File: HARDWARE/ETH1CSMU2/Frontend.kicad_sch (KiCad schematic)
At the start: 76 parts, among them Q601 MMBT3904, Q602 MMBT3904, Q603 MMBT3904, Q604 MMBT3904, U601 DG419DY, U602 DG419DY, U603 SN74LVC1T45DRLR, U604 SN74LVC1T45DRLR, U605 SN74LVC1T45DRLR, U606 LT1970ACFE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

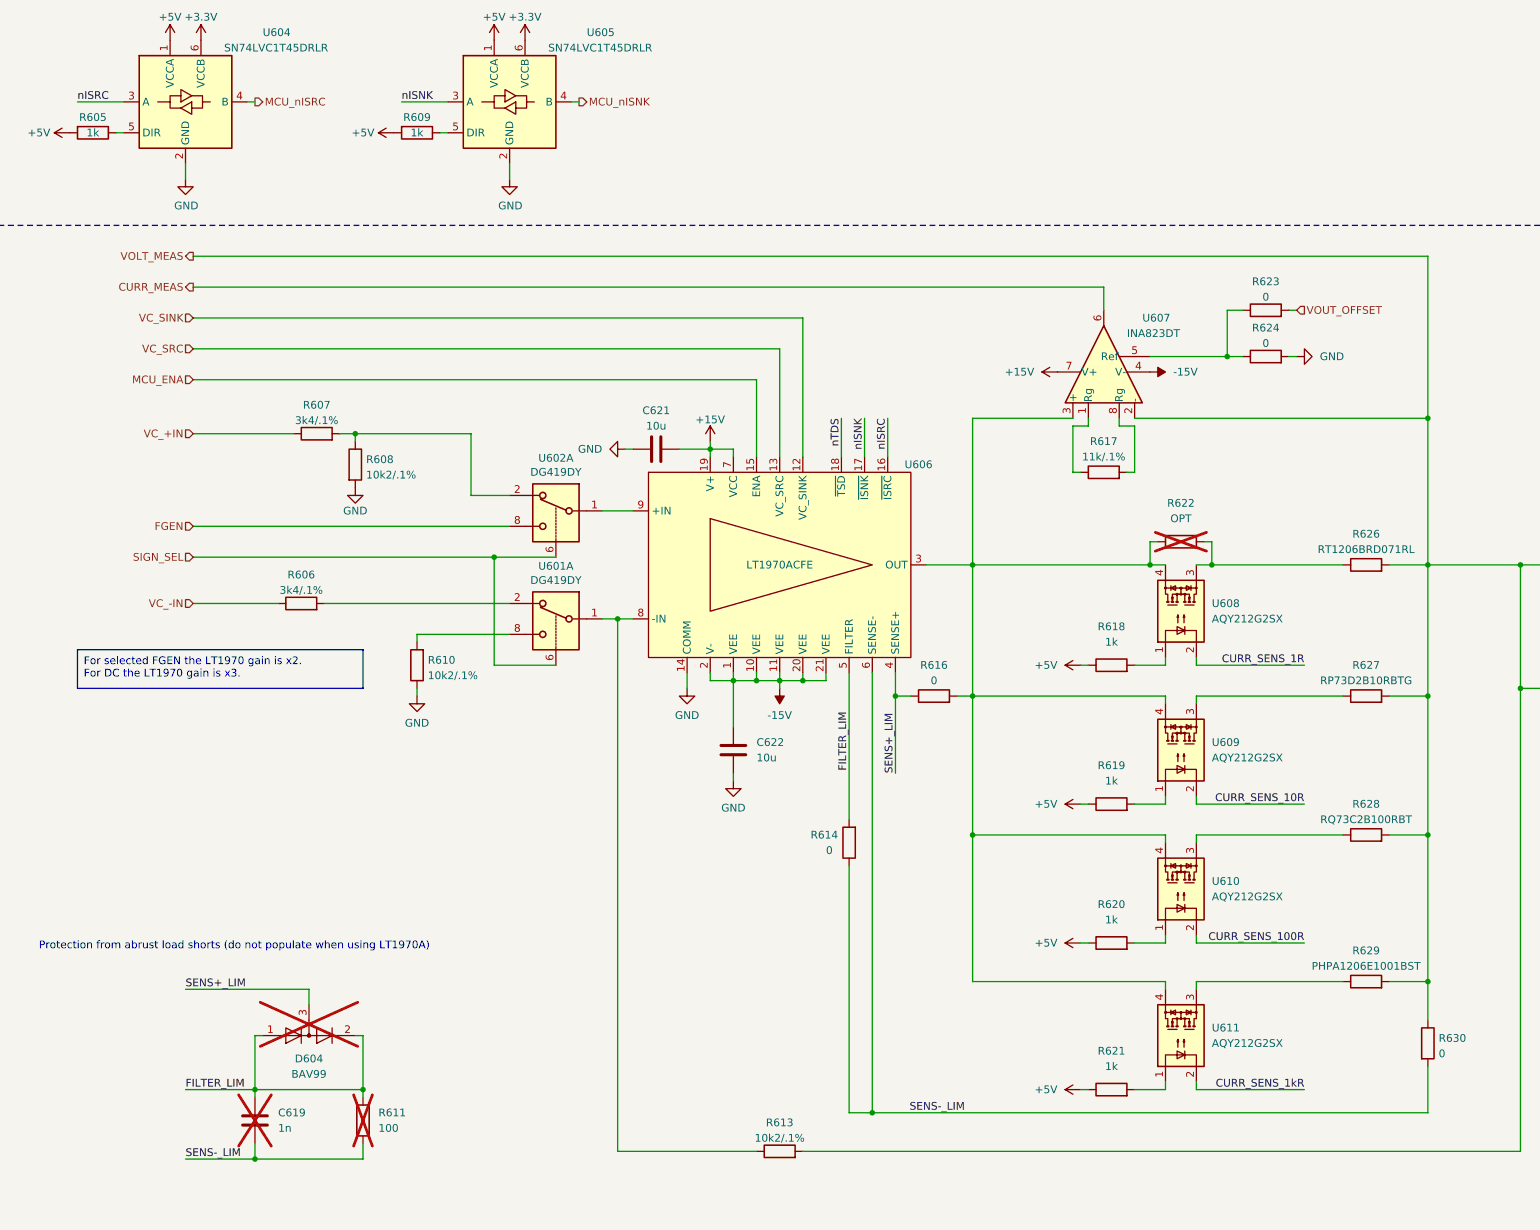
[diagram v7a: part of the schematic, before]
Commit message: Hardware fix. Created README file
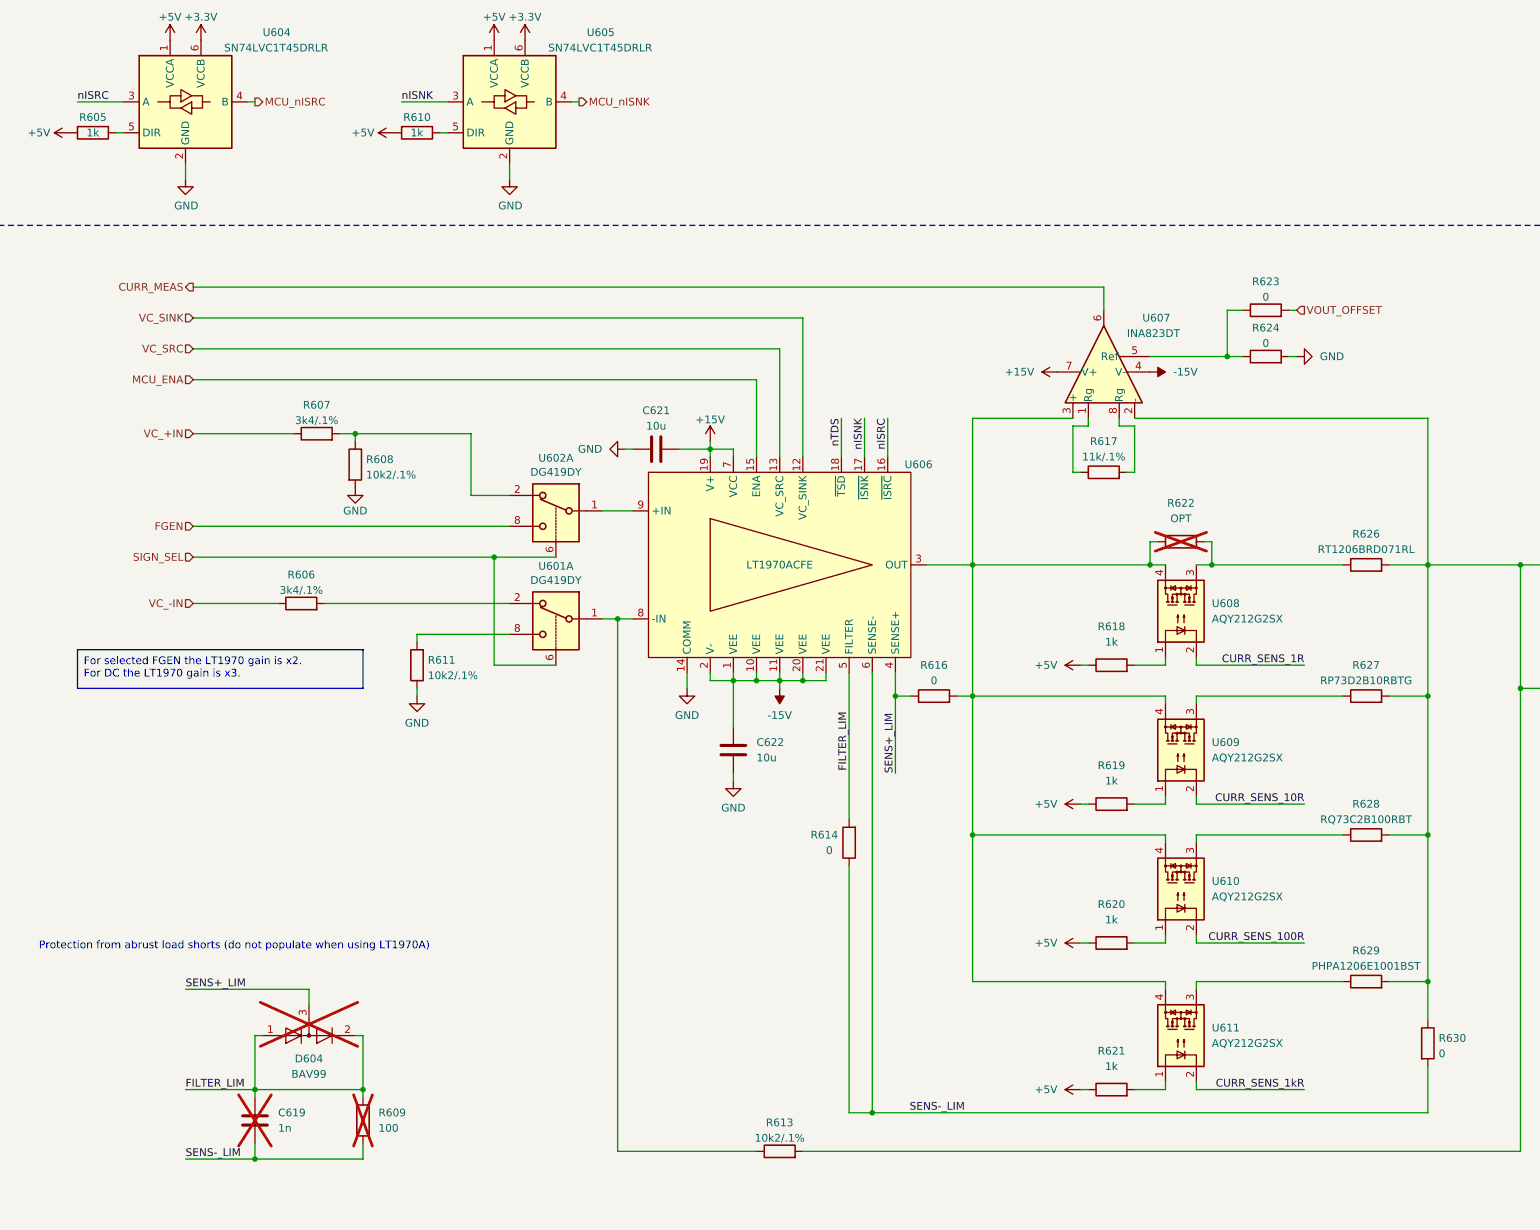
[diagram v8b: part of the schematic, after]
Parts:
- renumbered R611 to R609, R609 to R610, R610 to R611
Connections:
- net VOLT_MEAS renamed VOUT_OUT
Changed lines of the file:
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@@
 (kicad_sch (version 20230121) (generator eeschema)
   (paper "A3")
+  (title_block
+    (date "2023-07-12")
+    (rev "1.1")
+  )
   (junction (at 43.18 49.53) (diameter 0) (color 0 0 0 0)
   )
@@
   (junction (at 203.2 134.62) (diameter 0) (color 0 0 0 0)
   )
-  (junction (at 321.31 129.54) (diameter 0) (color 0 0 0 0)
-  )
   (junction (at 288.29 119.38) (diameter 0) (color 0 0 0 0)
   )
@@
     (stroke (width 0) (type default))
   )
-  (wire (pts (xy 321.31 129.54) (xy 321.31 102.87))
-    (stroke (width 0) (type default))
-  )
   (wire (pts (xy 118.11 113.03) (xy 218.44 113.03))
     (stroke (width 0) (type default))
@@
     (stroke (width 0) (type default))
   )
-  (wire (pts (xy 321.31 102.87) (xy 118.11 102.87))
-    (stroke (width 0) (type default))
-  )
   (wire (pts (xy 55.88 113.03) (xy 68.58 113.03))
     (stroke (width 0) (type default))
@@
     (effects (font (size 1.27 1.27)) (justify right))
   )
-  (hierarchical_label "VOLT_MEAS" (shape output) (at 118.11 102.87 180) (fields_autoplaced)
-    (effects (font (size 1.27 1.27)) (justify right))
-  )
   (hierarchical_label "SIGN_SEL" (shape input) (at 118.11 152.4 180) (fields_autoplaced)
     (effects (font (size 1.27 1.27)) (justify right))
@@
   (symbol (lib_id "Device:R") (at 154.94 82.55 270) (unit 1)
     (in_bom yes) (on_board yes) (dnp no)
-    (property "Reference" "R609" (at 154.94 80.01 90)
+    (property "Reference" "R610" (at 154.94 80.01 90)
       (effects (font (size 1.27 1.27)))
     )
@@
       (project "ETH1CSMU2"
         (path "/1fc6a863-b4aa-4691-87d2-d385f614c99b/3a644252-ed23-44df-80e7-4e1c292a7b4d"
-          (reference "R609") (unit 1)
+          (reference "R610") (unit 1)
         )
       )
@@
   (symbol (lib_id "Device:R") (at 154.94 170.18 180) (unit 1)
     (in_bom yes) (on_board yes) (dnp no) (fields_autoplaced)
-    (property "Reference" "R610" (at 156.718 169.3453 0)
+    (property "Reference" "R611" (at 156.718 169.3453 0)
       (effects (font (size 1.27 1.27)) (justify right))
     )
@@
       (project "ETH1CSMU2"
         (path "/1fc6a863-b4aa-4691-87d2-d385f614c99b/3a644252-ed23-44df-80e7-4e1c292a7b4d"
-          (reference "R610") (unit 1)
+          (reference "R611") (unit 1)
         )
       )
@@
   (symbol (lib_id "Device:R") (at 146.05 245.11 0) (unit 1)
     (in_bom yes) (on_board yes) (dnp yes) (fields_autoplaced)
-    (property "Reference" "R611" (at 148.59 243.8399 0)
+    (property "Reference" "R609" (at 148.59 243.8399 0)
       (effects (font (size 1.27 1.27)) (justify left))
     )
@@
       (project "ETH1CSMU2"
         (path "/1fc6a863-b4aa-4691-87d2-d385f614c99b/3a644252-ed23-44df-80e7-4e1c292a7b4d"
-          (reference "R611") (unit 1)
+          (reference "R609") (unit 1)
         )
       )
